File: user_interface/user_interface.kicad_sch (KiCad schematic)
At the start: 12 parts, among them J1 Conn_01x06, U1 ADS1115IDGS, U2 ADS1115IDGS, U3 TXS0101DCKR

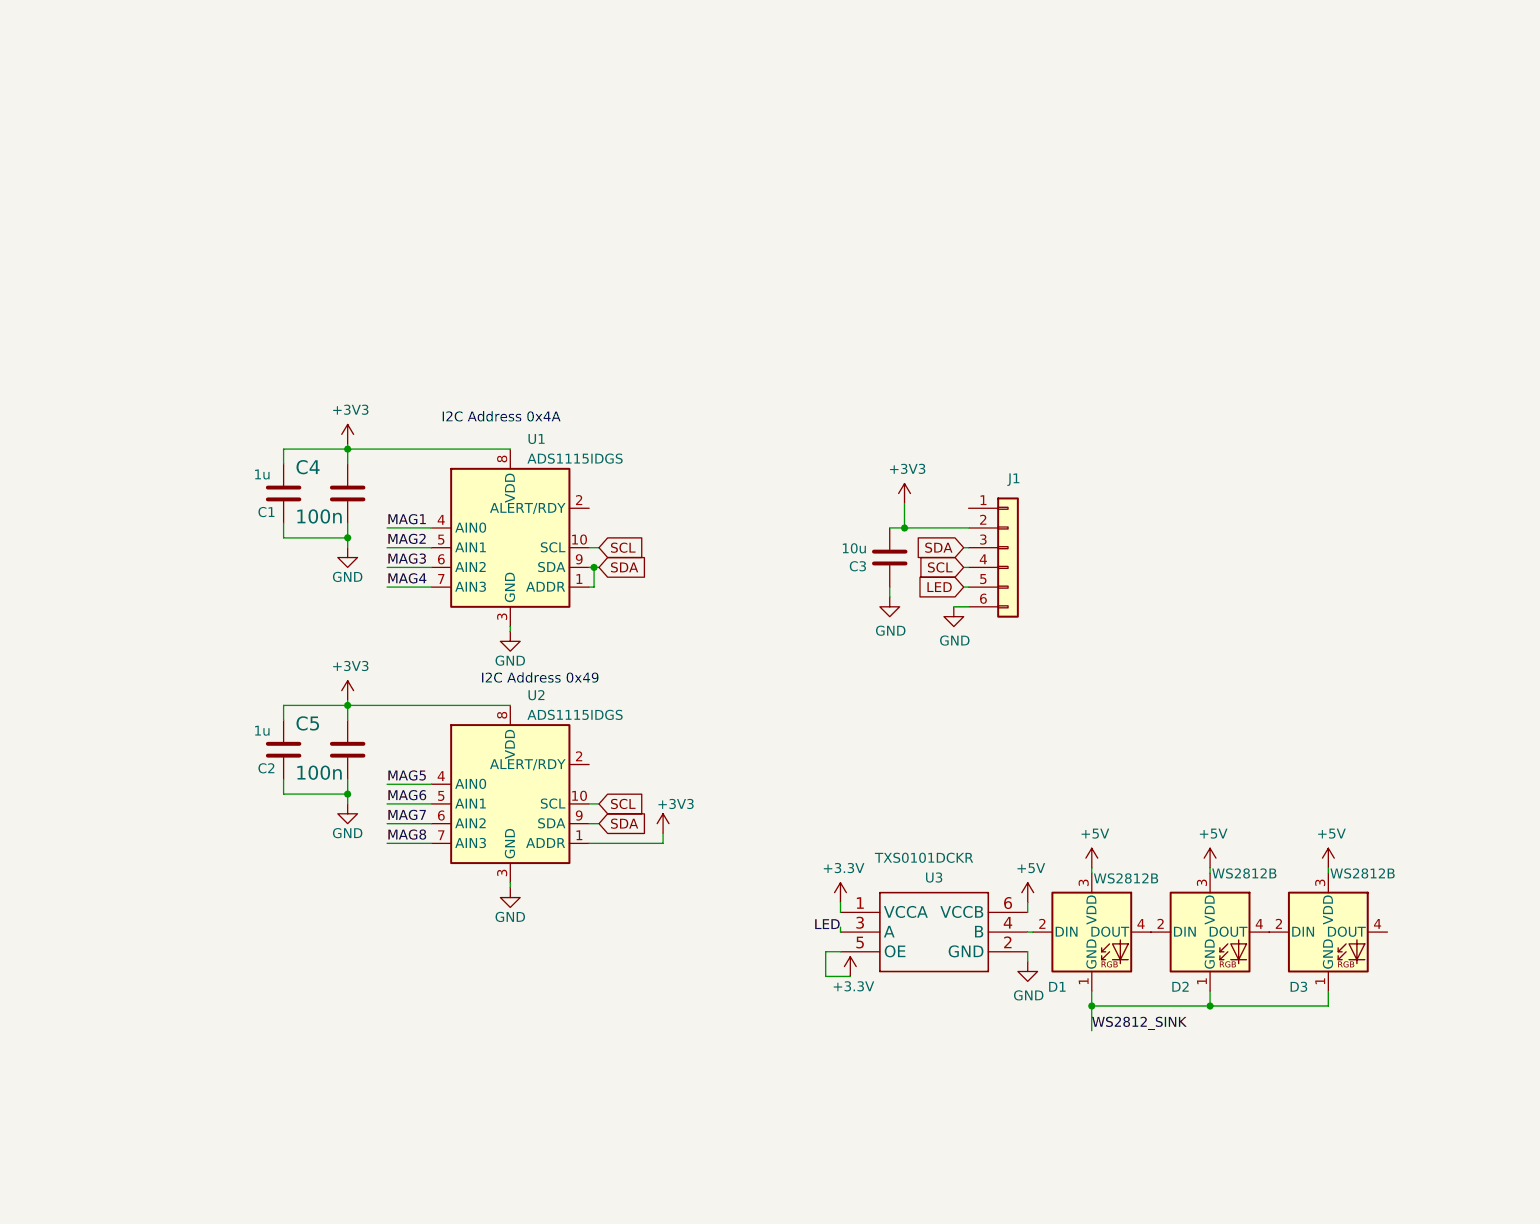
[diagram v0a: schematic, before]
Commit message: Mostly finished the User Interface PCB
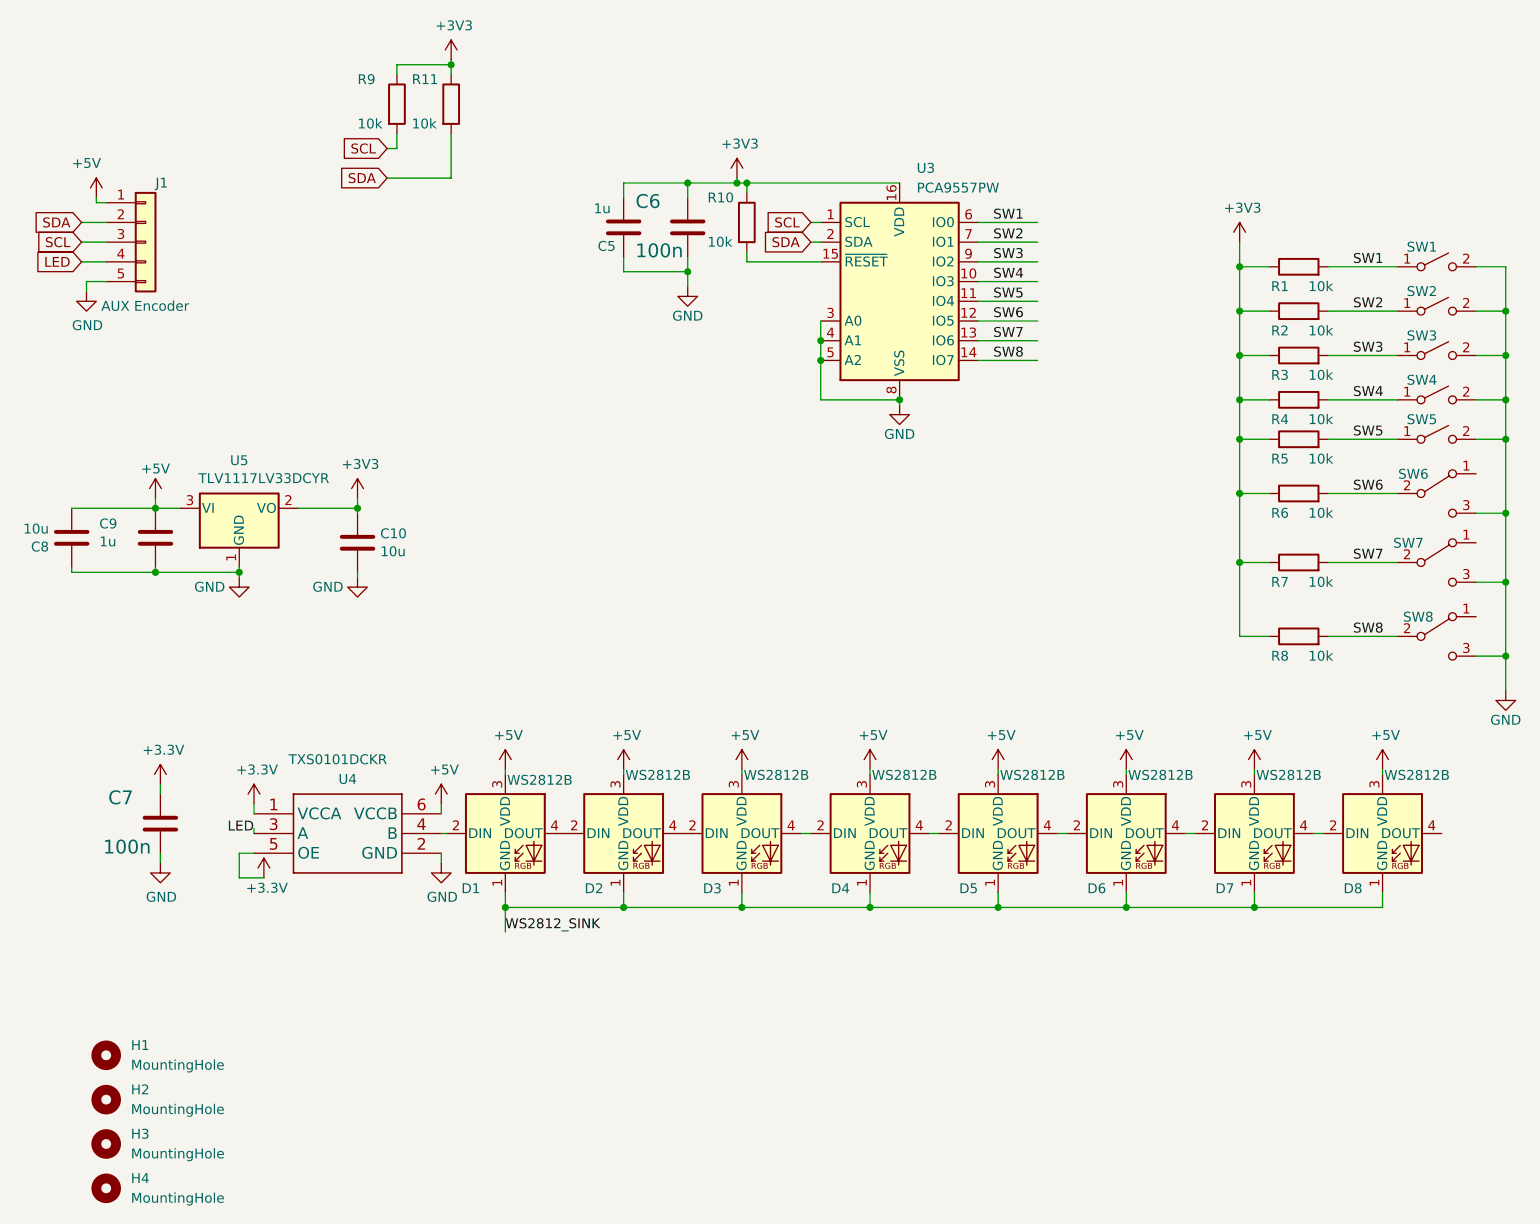
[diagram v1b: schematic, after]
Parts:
- removed C1, C2: 1u, Capacitor_SMD:C_0603_1608Metric, symbol Device:C
- removed C3: 10u, Capacitor_SMD:C_0805_2012Metric, symbol Device:C
- removed C4: 100n, Capacitor_SMD:C_0603_1608Metric, symbol Device:C
- removed J1: Conn_01x06, parts:Ckmtw-W-2510S06P_1x06_P2.54mm_Horizontal, symbol Connector_Generic:Conn_01x06
- removed U1, U2: ADS1115IDGS, Package_SO:TSSOP-10_3x3mm_P0.5mm, symbol Analog_ADC:ADS1115IDGS
- added C10, C8: 10u, Capacitor_SMD:C_0805_2012Metric, symbol Device:C
- added C6, C7: 100n, Capacitor_SMD:C_0603_1608Metric, symbol Device:C
- added C9: 1u, Capacitor_SMD:C_0603_1608Metric, symbol Device:C
- added D4, D5, D6, D7, D8: WS2812B, RP2040_minimal:LED_WS2812_3528_3.5x2.8mm_P1.5mm, symbol MotorBuck:WS2812B
- added H1, H2, H3, H4: MountingHole, RP2040_minimal:MountingHole_3.9mm_Plastite_#6, symbol Mechanical:MountingHole
- added J1: AUX Encoder, parts:CONN-TH_5P-P2.54_HCTL_HC-2510-5AW, symbol Connector_Generic:Conn_01x05
- added R1, R10, R11, R2, R3, R4, R5, R6, R7, R8, R9: 10k, Resistor_SMD:R_0603_1608Metric, symbol Device:R
- added SW1, SW2, SW3, SW4, SW5: SW_SPST, Button_Switch_SMD:SW_SPST_B3S-1000, symbol Switch:SW_SPST
- added SW6, SW7, SW8: SW_SPDT, parts:CS12ANW03, symbol Switch:SW_SPDT
- added U3: PCA9557PW, Package_SO:TSSOP-16_4.4x5mm_P0.65mm, symbol Interface_Expansion:PCA9557PW
- added U5: TLV1117LV33DCYR, Package_TO_SOT_SMD:SOT-223-3_TabPin2, symbol Regulator_Linear:NCP1117-3.3_SOT223
- C5: value 100n -> 1u; LCSC (none) -> C15849
- renumbered U3 to U4
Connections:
- net +3V3: now also C5.2, C10.1, C6.1, C7.1, R1.1, R10.1, R11.1, R2.1, R3.1, R4.1, R5.1, R6.1, R7.1, R8.1, R9.1, U3.16 (VDD), U5.2 (VO); no longer C5.1
- net +5V: now also C8.2, C9.1, D4.3 (VDD), D5.3 (VDD), D6.3 (VDD), D7.3 (VDD), D8.3 (VDD), J1.1 (Pin_1), U5.3 (VI)
- net GND: now also C5.1, C10.2, C6.2, C7.2, C8.1, C9.2, J1.5 (Pin_5), SW1.2 (B), SW2.2 (B), SW3.2 (B), SW4.2 (B), SW5.2 (B), SW6.3 (C), SW7.3 (C), SW8.3 (C), U3.3 (A0), U3.4 (A1), U3.5 (A2), U3.8 (VSS), U5.1 (GND); no longer C5.2
- net LED: now also J1.4 (Pin_4)
- net SCL: now also J1.3 (Pin_3), R9.2, U3.1 (SCL)
- net SDA: now also J1.2 (Pin_2), R11.2, U3.2 (SDA)
- net WS2812_SINK: now also D4.1 (GND), D5.1 (GND), D6.1 (GND), D7.1 (GND), D8.1 (GND)
- net at D3.4 (DOUT): now also D4.2 (DIN)
- new net: R10.2, U3.15 (~{RESET})
- new net: D4.4 (DOUT), D5.2 (DIN)
- new net: D5.4 (DOUT), D6.2 (DIN)
- new net: D6.4 (DOUT), D7.2 (DIN)
- new net: D7.4 (DOUT), D8.2 (DIN)
- new net SW1: R1.2, SW1.1 (A), U3.6 (IO0)
- new net SW2: R2.2, SW2.1 (A), U3.7 (IO1)
- new net SW3: R3.2, SW3.1 (A), U3.9 (IO2)
- new net SW4: R4.2, SW4.1 (A), U3.10 (IO3)
- new net SW5: R5.2, SW5.1 (A), U3.11 (IO4)
- new net SW6: R6.2, SW6.2 (B), U3.12 (IO5)
- new net SW7: R7.2, SW7.2 (B), U3.13 (IO6)
- new net SW8: R8.2, SW8.2 (B), U3.14 (IO7)
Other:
- note removed: "I2C Address 0x49"
- note removed: "I2C Address 0x4A"
- moved on the sheet: D1, D2, D3, U4

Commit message: Update user_interface pcb
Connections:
- net WS2812_SINK is gone; now on net GND: D1.1 (GND), D2.1 (GND), D3.1 (GND), D4.1 (GND), D5.1 (GND), D6.1 (GND), D7.1 (GND), D8.1 (GND)
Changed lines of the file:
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@@
-    (effects (font (size 1.27 1.27)) (justify left bottom))
-  )
-  (label "WS2812_SINK" (at 113.665 137.16 0) (fields_autoplaced)
     (effects (font (size 1.27 1.27)) (justify left bottom))
   )
@@
         )
       )
+    )
+  )
+  (symbol (lib_id "power:GND") (at 113.665 137.16 0) (unit 1)
+    (in_bom yes) (on_board yes) (dnp no)
+    (property "Reference" "#PWR05" (at 113.665 143.51 0)
+      (effects (font (size 1.27 1.27)) hide)
+    )
+    (property "Value" "GND" (at 113.792 141.5542 0)
+      (effects (font (size 1.27 1.27)))
+    )
+    (property "Footprint" "" (at 113.665 137.16 0)
+      (effects (font (size 1.27 1.27)) hide)
+    )
+    (property "Datasheet" "" (at 113.665 137.16 0)
+      (effects (font (size 1.27 1.27)) hide)
+    )
+    (pin "1")
+    (instances
+      (project "user_interface"
+        (path "/46ebe377-a663-4685-b60a-ebb47fe90031"
+          (reference "#PWR05") (unit 1)
+        )
+      )

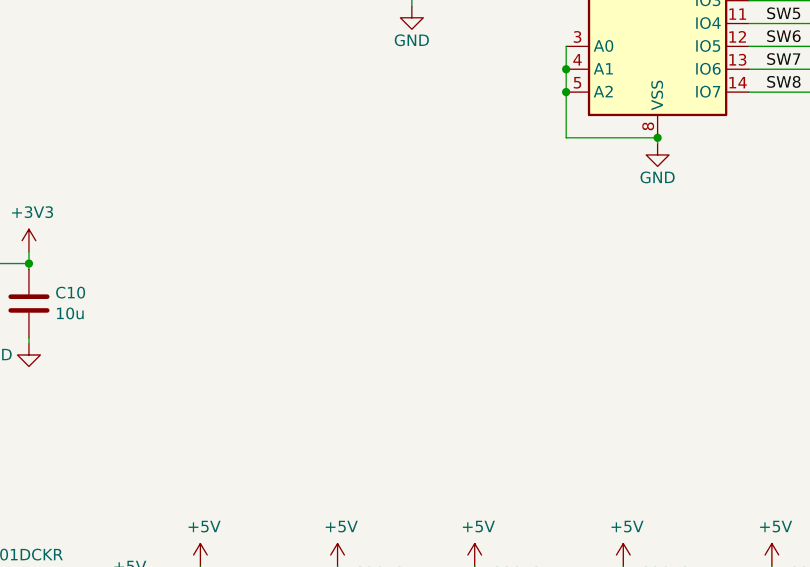
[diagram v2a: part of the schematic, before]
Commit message: Clean up of motor, base, and UI PCBs. Could be ready to order.
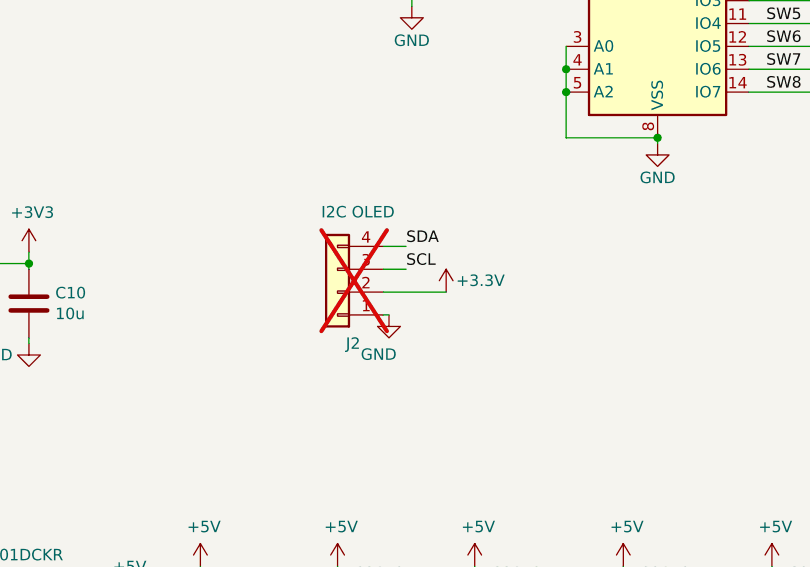
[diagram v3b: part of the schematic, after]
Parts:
- added J2: I2C OLED, Connector_PinHeader_2.54mm:PinHeader_1x04_P2.54mm_Vertical, symbol Connector_Generic:Conn_01x04
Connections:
- net +3V3: now also J2.2 (Pin_2)
- net GND: now also J2.1 (Pin_1)
- net SCL: now also J2.3 (Pin_3)
- net SDA: now also J2.4 (Pin_4)
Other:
- company: (none) -> Twisted Fields LLC
- title: (none) -> Motor User Interface PCB
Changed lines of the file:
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@@
 (kicad_sch (version 20230121) (generator eeschema)
   (paper "A4")
+  (title_block
+    (title "Motor User Interface PCB")
+    (date "2024-04-20")
+    (rev "1")
+    (company "Twisted Fields LLC")
+  )
   (junction (at 164.465 68.58) (diameter 0) (color 0 0 0 0)
   )
@@
     (stroke (width 0) (type default))
   )
+  (wire (pts (xy 136.525 80.645) (xy 133.985 80.645))
+    (stroke (width 0) (type default))
+  )
   (wire (pts (xy 238.76 57.15) (xy 242.57 57.15))
     (stroke (width 0) (type default))
@@
     (stroke (width 0) (type default))
   )
+  (wire (pts (xy 133.985 85.725) (xy 140.97 85.725))
+    (stroke (width 0) (type default))
+  )
   (wire (pts (xy 105.41 121.92) (xy 105.41 120.65))
     (stroke (width 0) (type default))
@@
     (stroke (width 0) (type default))
   )
+  (wire (pts (xy 134.62 88.265) (xy 133.985 88.265))
+    (stroke (width 0) (type default))
+  )
   (wire (pts (xy 144.78 49.53) (xy 144.78 50.8))
     (stroke (width 0) (type default))
@@
   )
   (wire (pts (xy 62.23 50.8) (xy 59.055 50.8))
+    (stroke (width 0) (type default))
+  )
+  (wire (pts (xy 136.525 83.185) (xy 133.985 83.185))
     (stroke (width 0) (type default))
   )
@@
     (effects (font (size 1.27 1.27)) (justify left bottom))
   )
+  (label "SCL" (at 136.525 83.185 0) (fields_autoplaced)
+    (effects (font (size 1.27 1.27)) (justify left bottom))
+  )
   (label "SW1" (at 176.53 45.72 0) (fields_autoplaced)
+    (effects (font (size 1.27 1.27)) (justify left bottom))
+  )
+  (label "SDA" (at 136.525 80.645 0) (fields_autoplaced)
     (effects (font (size 1.27 1.27)) (justify left bottom))
   )
@@
     )
   )
+  (symbol (lib_id "power:GND") (at 134.62 88.265 0) (unit 1)
+    (in_bom yes) (on_board yes) (dnp no)
+    (property "Reference" "#PWR06" (at 134.62 94.615 0)
+      (effects (font (size 1.27 1.27)) hide)
+    )
+    (property "Value" "GND" (at 133.477 92.6592 0)
+      (effects (font (size 1.27 1.27)))
+    )
+    (property "Footprint" "" (at 134.62 88.265 0)
+      (effects (font (size 1.27 1.27)) hide)
+    )
+    (property "Datasheet" "" (at 134.62 88.265 0)
+      (effects (font (size 1.27 1.27)) hide)
+    )
+    (pin "1")
+    (instances
+      (project "user_interface"
+        (path "/46ebe377-a663-4685-b60a-ebb47fe90031"
+          (reference "#PWR06") (unit 1)
+        )
+      )
+    )
+  )
   (symbol (lib_id "Switch:SW_SPST") (at 233.68 73.66 0) (unit 1)
     (in_bom yes) (on_board yes) (dnp no)
@@
         (path "/46ebe377-a663-4685-b60a-ebb47fe90031"
           (reference "SW4") (unit 1)
+        )
+      )
+    )
+  )
+  (symbol (lib_id "power:+3.3V") (at 140.97 85.725 0) (unit 1)
+    (in_bom yes) (on_board yes) (dnp no)
+    (property "Reference" "#PWR07" (at 140.97 89.535 0)
+      (effects (font (size 1.27 1.27)) hide)
+    )
+    (property "Value" "+3.3V" (at 144.78 84.455 0)
+      (effects (font (size 1.27 1.27)))
+    )
+    (property "Footprint" "" (at 140.97 85.725 0)
+      (effects (font (size 1.27 1.27)) hide)
+    )
+    (property "Datasheet" "" (at 140.97 85.725 0)
+      (effects (font (size 1.27 1.27)) hide)
+    )
+    (pin "1")
+    (instances
+      (project "user_interface"
+        (path "/46ebe377-a663-4685-b60a-ebb47fe90031"
+          (reference "#PWR07") (unit 1)
         )
       )
@@
         )
       )
+    )
+  )
+  (symbol (lib_id "Connector_Generic:Conn_01x04") (at 128.905 85.725 180) (unit 1)
+    (in_bom yes) (on_board yes) (dnp yes)
+    (property "Reference" "J2" (at 131.445 91.4401 0)
+      (effects (font (size 1.27 1.27)) (justify left))
+    )
+    (property "Value" "I2C OLED" (at 135.255 76.8351 0)
+      (effects (font (size 1.27 1.27)) (justify left))
+    )
+    (property "Footprint" "Connector_PinHeader_2.54mm:PinHeader_1x04_P2.54mm_Vertical" (at 128.905 85.725 0)
+      (effects (font (size 1.27 1.27)) hide)
+    )
+    (property "Datasheet" "https://datasheet.lcsc.com/lcsc/1912111437_PINREX-744-81-04TW00_C402777.pdf" (at 128.905 85.725 0)
+      (effects (font (size 1.27 1.27)) hide)
+    )
+    (property "LCSC" "" (at 128.905 85.725 0)
+      (effects (font (size 1.27 1.27)) hide)
+    )
+    (pin "1")
+    (pin "2")
+    (pin "3")
+    (pin "4")
+    (instances
+      (project "user_interface"
+        (path "/46ebe377-a663-4685-b60a-ebb47fe90031"
+          (reference "J2") (unit 1)
+        )
+      )

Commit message: Final files as ordered today for base, module, and UI
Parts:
- J2: now left out of the parts list
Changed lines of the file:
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@@
   )
   (symbol (lib_id "Connector_Generic:Conn_01x04") (at 128.905 85.725 180) (unit 1)
-    (in_bom yes) (on_board yes) (dnp yes)
+    (in_bom no) (on_board yes) (dnp yes)
     (property "Reference" "J2" (at 131.445 91.4401 0)
       (effects (font (size 1.27 1.27)) (justify left))
